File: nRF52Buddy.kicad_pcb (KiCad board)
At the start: 4 copper layers, 60 x 35 mm, 94 parts, among them J1 2060-452_998-404, J2 SWD, J3 2305018-2, J4 Conn_02x26_Odd_Even, J5 Conn_02x26_Odd_Even, J6 HDGC1251WR-S-2P, Q1 SSM3J332R, Q2 SSM3J332R, Q3 SSM3J332R, SW1 SW_SPST, U1 AP9211, U2 MAX17260SETD, U3 TP4054, U4 TP6841S6, U5 MIC5205-3.3YM5, U6 MDBT50Q-1MV2, U7 USBLC6-2SC6, Y1 32.768 kHz

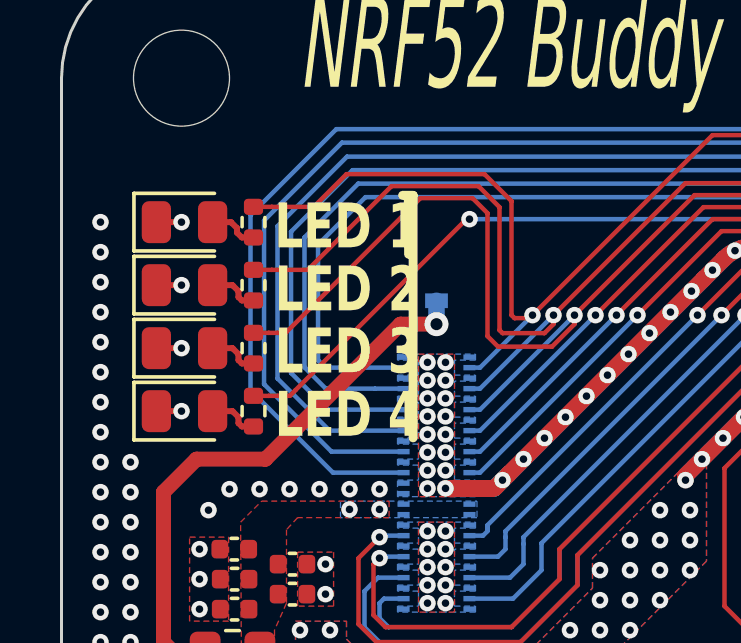
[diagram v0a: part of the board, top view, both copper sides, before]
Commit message: updating indicator LED position and silkscreen
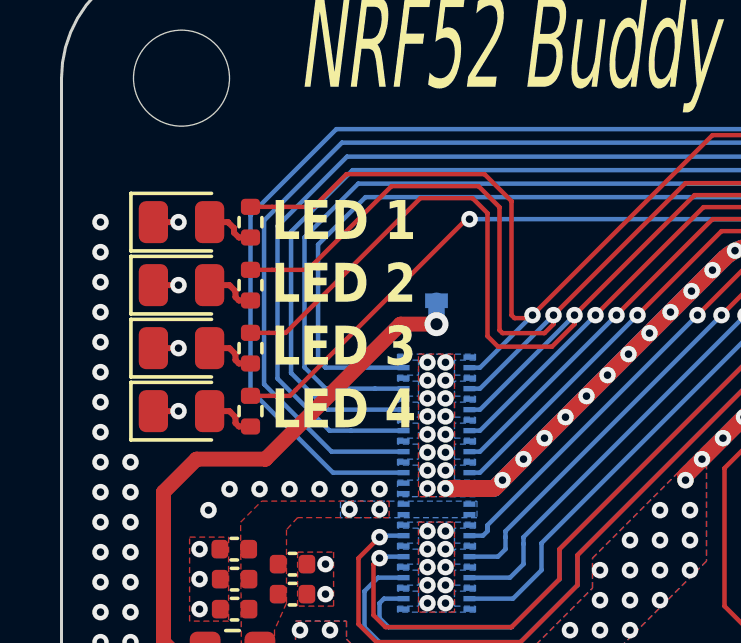
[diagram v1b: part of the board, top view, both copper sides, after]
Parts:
- moved R11 0.10 mm to (76.3, 101.0)
- moved R12 0.10 mm to (76.3, 107.3)
- moved R14 0.10 mm to (76.3, 103.1)
- moved R18 0.10 mm to (76.3, 105.2)
- moved D10 0.10 mm to (74.0, 105.2)
- moved D7 0.10 mm to (74.0, 101.0)
- moved D8 0.10 mm to (74.0, 107.3)
- moved D9 0.10 mm to (74.0, 103.1)
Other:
- board text added: "LED 1 LED 2 LED 3 LED 4"
- board text removed: "LED 1"
- board text removed: "LED 2"
- board text removed: "LED 3"
- board text removed: "LED 4"

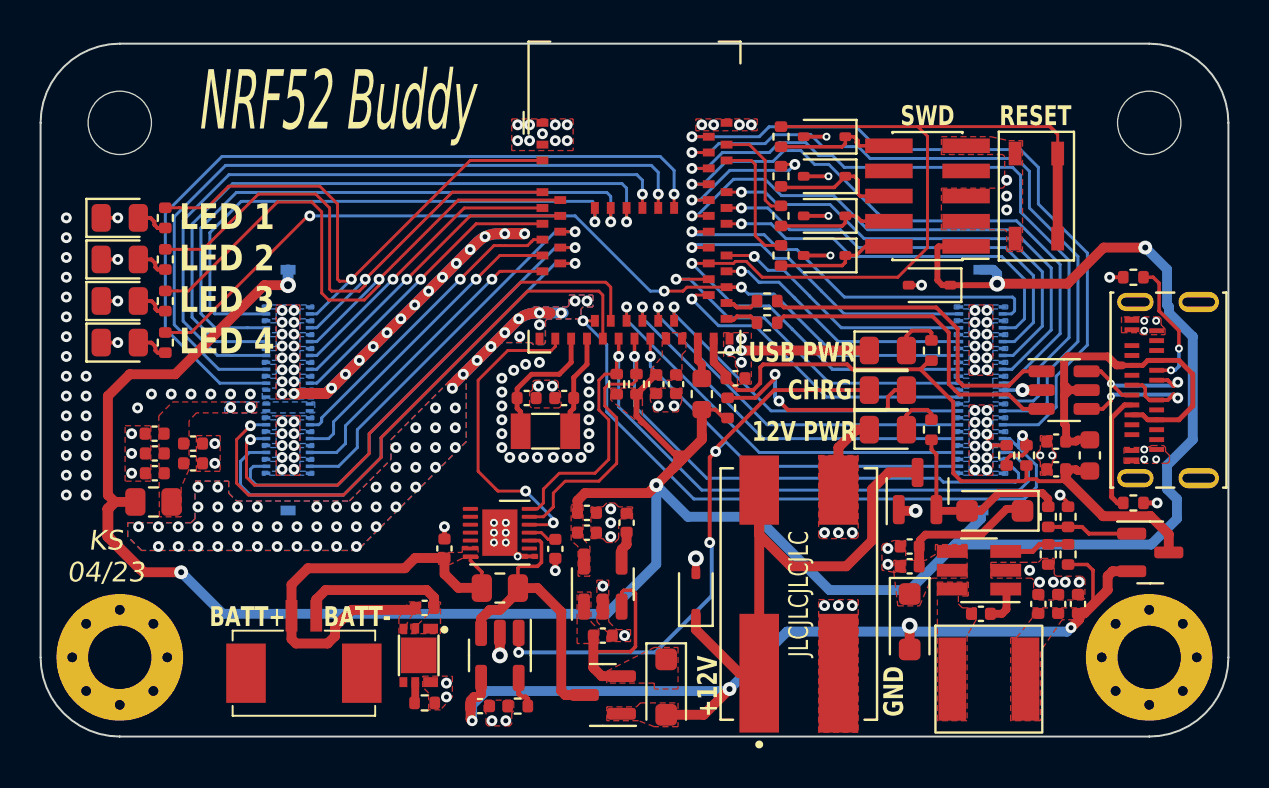
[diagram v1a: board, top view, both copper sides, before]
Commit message: Moving USB PWR, CHARG, and 12V LEDs further to left
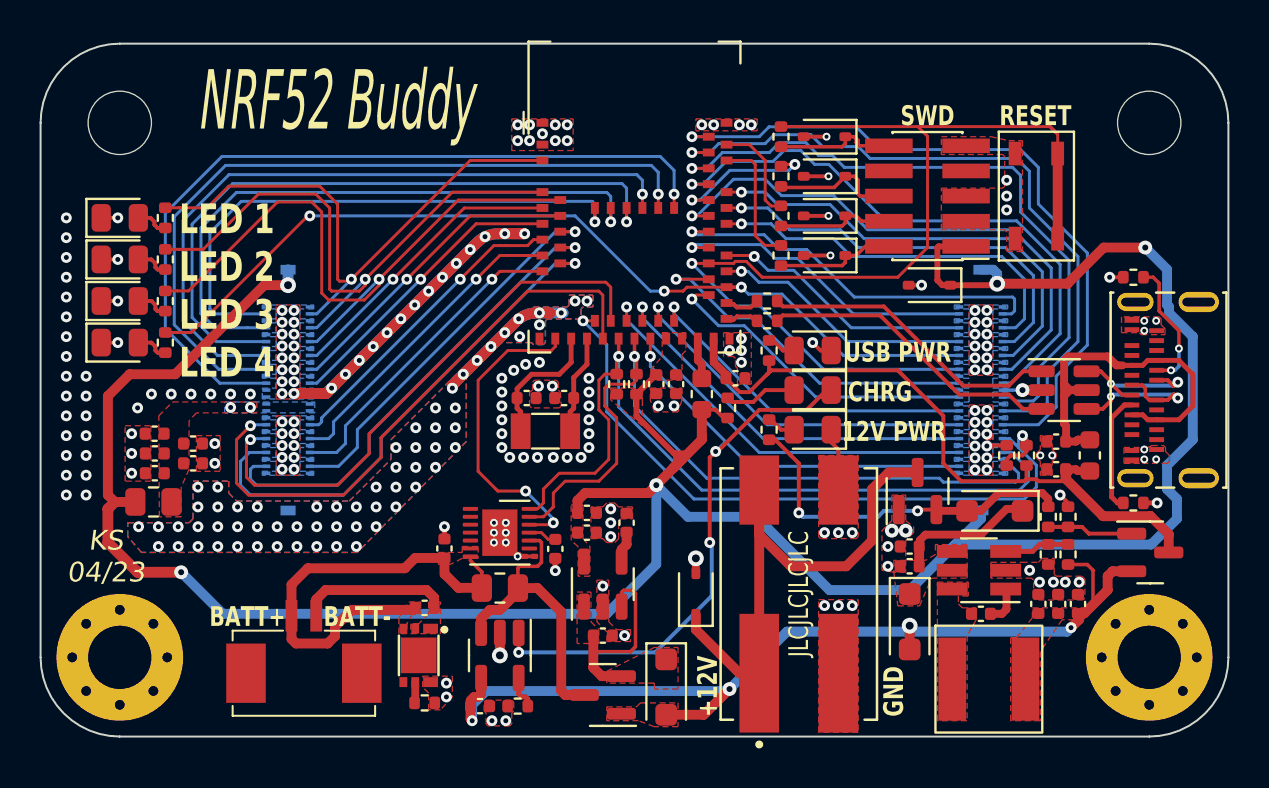
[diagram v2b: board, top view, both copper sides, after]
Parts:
- moved R21 8.20 mm to (106.8, 107.7)
- moved R22 8.20 mm to (106.8, 111.7)
- moved D12 3.80 mm to (109.0, 107.7), turned to 180 degrees
- moved D13 3.80 mm to (109.0, 111.7), turned to 180 degrees
- moved D16 3.80 mm to (109.0, 109.7), turned to 180 degrees
- moved R15 0.10 mm to (106.7, 106.2)
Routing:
- net Net-(D16-A): track 11.8 -> 3.70 mm, vias 2 -> 0
- net /Power Input/+12V: track 10.1 -> 18.2 mm, vias 0 -> 2
- net GND: track 76.7 -> 69.7 mm, vias 260 -> 262
- net /P1.09/~{CHARGE}: track 48.3 -> 46.5 mm
- net /MCU (nRF52840)/USB_D+: track 16.9 -> 15.5 mm
- net /MCU (nRF52840)/USB_D-: track 16.9 -> 15.7 mm
- net /Power Switching/V_USB_FILT: track 36.7 -> 35.4 mm
- net Net-(D12-A): track 2.54 -> 1.47 mm
- net Net-(D13-A): track 2.48 -> 1.47 mm
- net /MCU (nRF52840)/P0.13/BT_STATUS_LED: track 47.3 -> 46.3 mm

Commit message: Moving some tracks and increasing via diameter to allow for latest JLCPCB capabilities
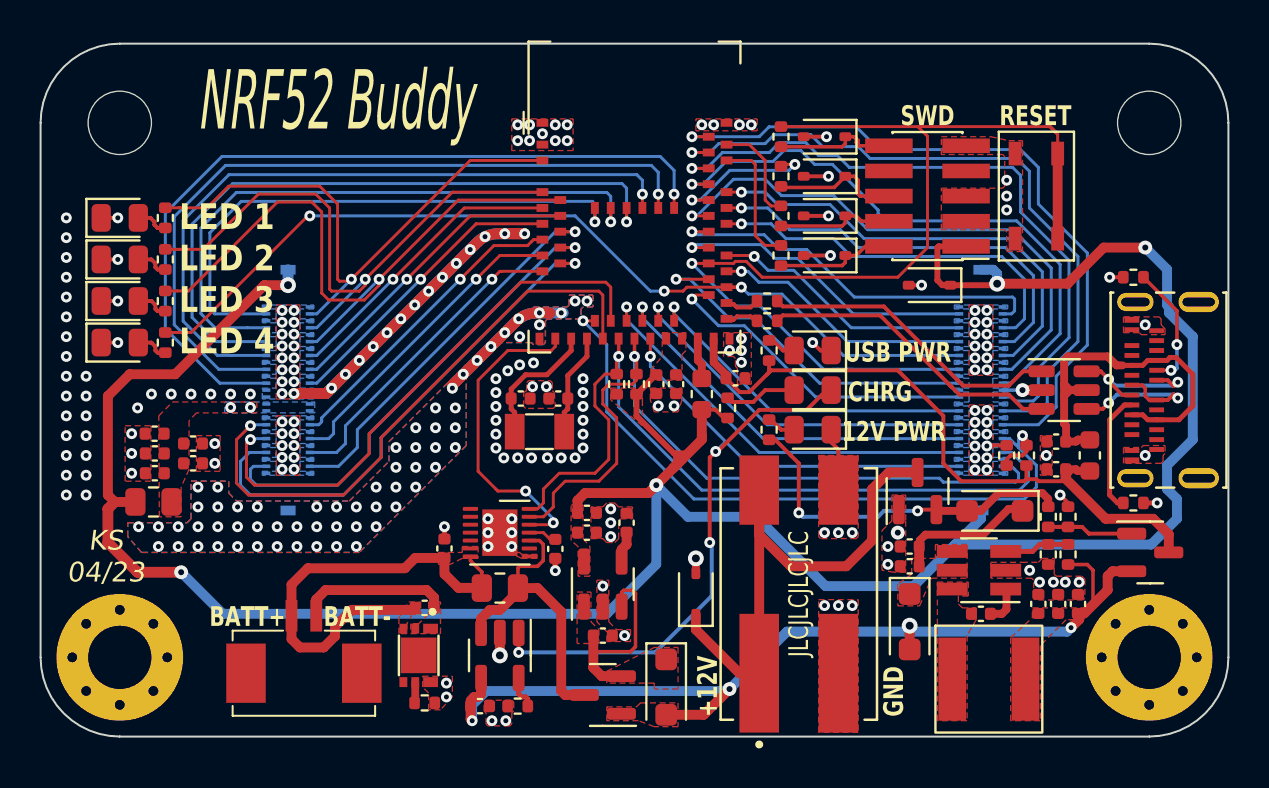
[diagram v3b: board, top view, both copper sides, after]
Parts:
- U1: footprint AP9211SA-AK-HAC-7:DFN200X300X60-7N -> Footprints:DFN200X300X60-7N
- moved C21 0.30 mm to (94.2, 110.1)
- moved C22 0.30 mm to (96.2, 110.1)
- moved Y1 0.30 mm to (95.2, 111.8)
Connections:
- net /Connectors/P0.26 renamed /Connectors/P0.26/V_USB_CONNECTED
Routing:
- net GND: track 69.7 -> 69.6 mm, vias 262 -> 255

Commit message: Updates for revision 3
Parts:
- removed D2: D_TVS_5V, Diode_SMD:D_SOD-323
- moved R7 1.11 mm to (76.6, 116.0), turned to -90 degrees
- moved C5 0.34 mm to (95.9, 117.4)
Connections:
- net /Connectors/P1.10 renamed /Connectors/P1.10/STATUS_LED1
- net /Connectors/P1.11 renamed /Connectors/P1.11/STATUS_LED2
- net /Connectors/P1.12 renamed /Connectors/P1.12/STATUS_LED3
- net /MCU (nRF52840)/P0.13/BT_STATUS_LED renamed /MCU (nRF52840)/P0.13/STATUS_LED4
- D16 pad 1: /P1.09/~{CHARGE} -> Net-(D16-K)
- J2 pad 1: +3V3 -> unconnected-(J2-Pin_1-Pad1)
- J4 pad 48: /P1.09/~{CHARGE} -> /Connectors/P1.09/~{CHARGE}
- J5 pad 52: +3V3 -> GND
- R32 pad 2: +3V3 -> +5V
- U2 pad 1: unconnected-(U2-TH-Pad1) -> /Power Input/BATT_CONN+
- U2 pad 9: unconnected-(U2-CSPL-Pad9) -> GND
- U3 pad 1: /P1.09/~{CHARGE} -> Net-(D16-K)
- U6 pad 26: /P1.09/~{CHARGE} -> /MCU (nRF52840)/P1.09
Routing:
- net /P1.09/~{CHARGE}: track 46.3 -> 0.00 mm, vias 4 -> 0
- net +3V3: track 137.5 -> 105.1 mm, vias 5 -> 4
- net Net-(D16-K): track 0.00 -> 26.4 mm, vias 0 -> 2
- net (no net): track 0.00 -> 19.1 mm, vias 0 -> 1
- net +5V: track 48.8 -> 65.1 mm
- net /Power Input/BATT_CONN+: track 23.4 -> 32.0 mm
- net /Power Input/BATT+: track 15.3 -> 18.8 mm
- net /MCU (nRF52840)/P0.27/FUEL_ALRT: track 15.9 -> 16.4 mm
- net GND: track 69.6 -> 69.1 mm, vias 255 -> 250
